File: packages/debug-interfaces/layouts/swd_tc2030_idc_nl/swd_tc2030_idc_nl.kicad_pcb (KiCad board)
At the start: 2 copper layers, 1 part

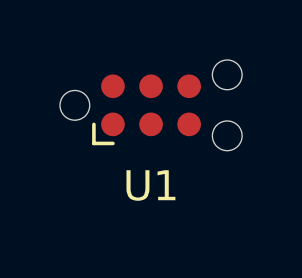
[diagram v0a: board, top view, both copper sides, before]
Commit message: Build all packages without designators on silkscreen.
Also disable fail_on_drc and enable keep_picked_parts for build
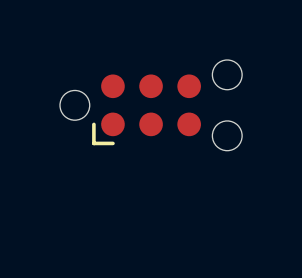
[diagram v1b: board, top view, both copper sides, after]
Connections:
- U1 pad 2: line -> line-3
- U1 pad 3: line-3 -> line
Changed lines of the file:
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@@
     (net 0 "")
     (net 1 "gnd")
-    (net 2 "line-3")
+    (net 2 "line")
     (net 3 "hv")
-    (net 4 "line")
+    (net 4 "line-3")
     (net 5 "line-1")
     (net 6 "line-2")
@@
             (at 0 2.7 0)
             (layer "F.SilkS")
-            (hide no)
+            (hide yes)
             (effects
                 (font
@@
                     (thickness 0.15)
                 )
+                (hide yes)
             )
             (unlocked no)
@@
             (size 0.7874 0.7874)
             (layers "F.Cu" "F.Mask")
-            (net 4 "line")
+            (net 4 "line-3")
         )
         (pad "3" connect circle
@@
             (size 0.7874 0.7874)
             (layers "F.Cu" "F.Mask")
-            (net 2 "line-3")
+            (net 2 "line")
         )
         (pad "4" connect circle

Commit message: [Publish] Rebuild modules (with no dep on upstream atopile pr) (#5)
* Fixes image link on published packages
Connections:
- U1 pad 2: line-3 -> line-1
- U1 pad 3: line -> line-3
- U1 pad 4: line-1 -> line
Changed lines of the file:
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@@
     (net 0 "")
     (net 1 "gnd")
-    (net 2 "line")
+    (net 2 "line-3")
     (net 3 "hv")
-    (net 4 "line-3")
-    (net 5 "line-1")
+    (net 4 "line-1")
+    (net 5 "line")
     (net 6 "line-2")
     (footprint "Connector:Tag-Connect_TC2030-IDC-NL_2x03_P1.27mm_Vertical"
@@
             (size 0.7874 0.7874)
             (layers "F.Cu" "F.Mask")
-            (net 4 "line-3")
+            (net 4 "line-1")
         )
         (pad "3" connect circle
@@
             (size 0.7874 0.7874)
             (layers "F.Cu" "F.Mask")
-            (net 2 "line")
+            (net 2 "line-3")
         )
         (pad "4" connect circle
@@
             (size 0.7874 0.7874)
             (layers "F.Cu" "F.Mask")
-            (net 5 "line-1")
+            (net 5 "line")
         )
         (pad "5" connect circle

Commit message: Rebuild all
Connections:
- U1 pad 2: line-1 -> line
- U1 pad 3: line-3 -> line-1
- U1 pad 4: line -> line-2
- U1 pad 6: line-2 -> line-3
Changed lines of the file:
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@@
     (net 0 "")
     (net 1 "gnd")
-    (net 2 "line-3")
+    (net 2 "line-1")
     (net 3 "hv")
-    (net 4 "line-1")
-    (net 5 "line")
-    (net 6 "line-2")
+    (net 4 "line")
+    (net 5 "line-2")
+    (net 6 "line-3")
     (footprint "Connector:Tag-Connect_TC2030-IDC-NL_2x03_P1.27mm_Vertical"
         (layer "F.Cu")
@@
             (size 0.7874 0.7874)
             (layers "F.Cu" "F.Mask")
-            (net 4 "line-1")
+            (net 4 "line")
         )
         (pad "3" connect circle
@@
             (size 0.7874 0.7874)
             (layers "F.Cu" "F.Mask")
-            (net 2 "line-3")
+            (net 2 "line-1")
         )
         (pad "4" connect circle
@@
             (size 0.7874 0.7874)
             (layers "F.Cu" "F.Mask")
-            (net 5 "line")
+            (net 5 "line-2")
         )
         (pad "5" connect circle
@@
             (size 0.7874 0.7874)
             (layers "F.Cu" "F.Mask")
-            (net 6 "line-2")
+            (net 6 "line-3")
         )
         (embedded_fonts no)

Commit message: Update packages to ato v0.9.x (#36)
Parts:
- removed U1: , Connector:Tag-Connect_TC2030-IDC-NL_2x03_P1.27mm_Vertical
- added TC1: , Tag_Connect_TC2030_IDC_NL_2x03_P1_27mm_Vertical:Tag_Connect_TC2030_IDC_NL_2x03_P1_27mm_Vertical, F.Cu at (0.00, 0.00)
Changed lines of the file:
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@@
     (version 20241229)
     (generator "atopile")
-    (generator_version "0.3.24")
+    (generator_version "0.9.1")
     (general
         (thickness 1.6)
@@
     )
     (net 0 "")
-    (net 1 "gnd")
-    (net 2 "line-1")
-    (net 3 "hv")
-    (net 4 "line")
-    (net 5 "line-2")
-    (net 6 "line-3")
-    (footprint "Connector:Tag-Connect_TC2030-IDC-NL_2x03_P1.27mm_Vertical"
+    (net 1 "connector.footprint.footprint.pins[1].net-net")
+    (net 2 "connector.footprint.footprint.pins[4].net-net")
+    (net 3 "connector.footprint.footprint.pins[3].net-net")
+    (net 4 "connector.footprint.footprint.pins[5].net-net")
+    (net 5 "connector.footprint.footprint.pins[2].net-net")
+    (net 6 "connector.footprint.footprint.pins[0].net-net")
+    (net 7 "connector.footprint.footprint.pins[6].net-net")
+    (footprint "Tag_Connect_TC2030_IDC_NL_2x03_P1_27mm_Vertical:Tag_Connect_TC2030_IDC_NL_2x03_P1_27mm_Vertical"
         (layer "F.Cu")
         (at 0 0 0)
-        (property "Reference" "U1"
+        (property "Reference" "TC1"
             (at 0 2.7 0)
             (layer "F.SilkS")
@@
             )
         )
-        (property "__atopile_lib_fp_hash__" "c8c98225-f34a-cddd-b1dc-1d9f3449ec6e"
+        (property "__atopile_lib_fp_hash__" "fc6086fa-b799-2df5-1018-17fd54d41ea9"
             (at 0 0 0)
             (layer "User.9")
@@
             )
         )
-        (property "atopile_address" "connector"
+        (property "atopile_address" "connector.footprint"
             (at 0 0 0)
             (layer "User.9")
@@
             (drill 0.9906)
             (layers "*.Cu" "*.Mask")
+            (net 6 "connector.footprint.footprint.pins[0].net-net")
         )
         (pad "" np_thru_hole circle
@@
             (drill 0.9906)
             (layers "*.Cu" "*.Mask")
+            (net 6 "connector.footprint.footprint.pins[0].net-net")
         )
         (pad "" np_thru_hole circle
@@
             (drill 0.9906)
             (layers "*.Cu" "*.Mask")
+            (net 6 "connector.footprint.footprint.pins[0].net-net")
         )
         (pad "1" connect circle
@@
             (size 0.7874 0.7874)
             (layers "F.Cu" "F.Mask")
-            (net 3 "hv")
+            (net 1 "connector.footprint.footprint.pins[1].net-net")
         )
         (pad "2" connect circle
@@
             (size 0.7874 0.7874)
             (layers "F.Cu" "F.Mask")
-            (net 4 "line")
+            (net 5 "connector.footprint.footprint.pins[2].net-net")
         )
         (pad "3" connect circle
@@
             (size 0.7874 0.7874)
             (layers "F.Cu" "F.Mask")
-            (net 2 "line-1")
+            (net 3 "connector.footprint.footprint.pins[3].net-net")
         )
         (pad "4" connect circle
@@
             (size 0.7874 0.7874)
             (layers "F.Cu" "F.Mask")
-            (net 5 "line-2")
+            (net 2 "connector.footprint.footprint.pins[4].net-net")
         )
         (pad "5" connect circle
@@
             (size 0.7874 0.7874)
             (layers "F.Cu" "F.Mask")
-            (net 1 "gnd")
+            (net 4 "connector.footprint.footprint.pins[5].net-net")
         )
         (pad "6" connect circle
@@
             (size 0.7874 0.7874)
             (layers "F.Cu" "F.Mask")
-            (net 6 "line-3")
+            (net 7 "connector.footprint.footprint.pins[6].net-net")
         )
         (embedded_fonts no)
